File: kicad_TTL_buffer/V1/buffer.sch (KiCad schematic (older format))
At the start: 19 parts, among them P1 Conn_02x06_Odd_Even, P2 Conn_01x04, P3 Conn_01x06, P4 Conn_01x03_ODD, P5 Conn_01x03_EVEN, P6 Conn_01x01, P7 Conn_01x01, U1 74LS08

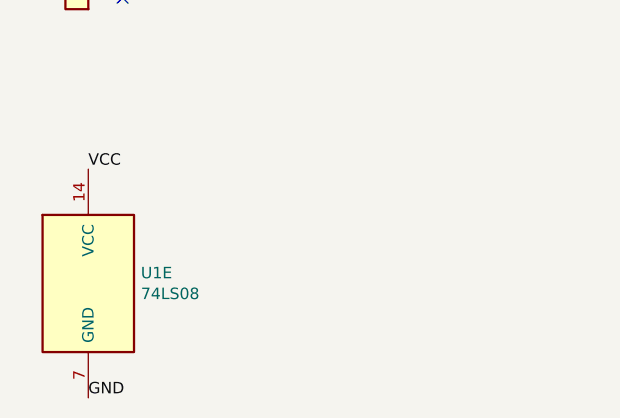
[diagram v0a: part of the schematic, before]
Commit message: Update TTL V1 board
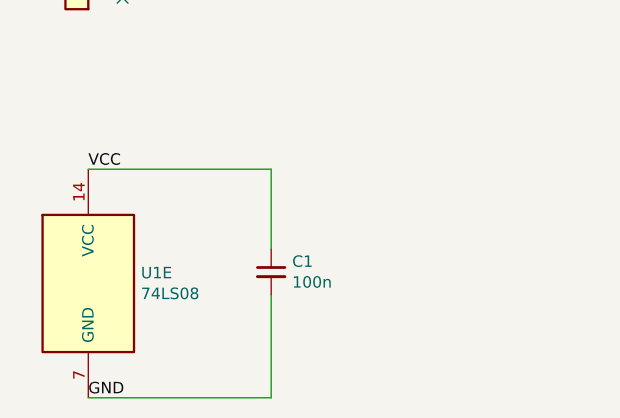
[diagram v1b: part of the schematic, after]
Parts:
- added C1: 100n, Capacitor_SMD:C_0805_2012Metric_Pad1.15x1.40mm_HandSolder, symbol Device:C_Small
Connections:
- net GND: now also C1.2
- net VCC: now also C1.1
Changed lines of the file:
@@
 Text Notes 850  4200 0    50   ~ 0
 R5 Not Fitted
+$Comp
+L Device:C_Small C1
+U 1 1 5E5AAE44
+P 1950 6250
+F 0 "C1" H 2042 6296 50  0000 L CNN
+F 1 "100n" H 2042 6205 50  0000 L CNN
+F 2 "Capacitor_SMD:C_0805_2012Metric_Pad1.15x1.40mm_HandSolder" H 1950 6250 50  0001 C CNN
+F 3 "~" H 1950 6250 50  0001 C CNN
+	1    1950 6250
+	1    0    0    -1
+$EndComp
+Wire Wire Line
+	1150 5800 1950 5800
+Wire Wire Line
+	1950 5800 1950 6150
+Wire Wire Line
+	1150 6800 1950 6800
+Wire Wire Line
+	1950 6800 1950 6350
 $EndSCHEMATC

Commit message: Extend P4 pads on TTL board
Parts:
- P3: footprint Connector_Molex:Molex_PicoBlade_53048-0610_1x06_P1.25mm_Horizontal -> Connector_Molex:Molex_PicoBlade_53048-0610_1x06_P1.25mm_Horizontal_Custom2
- P4: footprint Connector_Harwin:Harwin_M20-89003xx_1x03_P2.54mm_Horizontal_Custom_ODD -> Connector_Harwin:Harwin_M20-89003xx_1x03_P2.54mm_Horizontal_Custom_ODD2
- P5: footprint Connector_Harwin:Harwin_M20-89003xx_1x03_P2.54mm_Horizontal_Custom_EVEN -> Connector_Harwin:Harwin_M20-89003xx_1x03_P2.54mm_Horizontal_Custom_EVEN2
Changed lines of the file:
@@
 F 0 "P3" H 2168 3275 50  0000 C CNN
 F 1 "Conn_01x06" H 2168 3366 50  0000 C CNN
-F 2 "Connector_Molex:Molex_PicoBlade_53048-0610_1x06_P1.25mm_Horizontal" H 2250 3800 50  0001 C CNN
+F 2 "Connector_Molex:Molex_PicoBlade_53048-0610_1x06_P1.25mm_Horizontal_Custom2" H 2250 3800 50  0001 C CNN
 F 3 "~" H 2250 3800 50  0001 C CNN
 	1    2250 3800
@@
 F 0 "P5" H 1750 2850 50  0000 C CNN
 F 1 "Conn_01x03_EVEN" H 1450 2950 50  0000 C CNN
-F 2 "Connector_Harwin:Harwin_M20-89003xx_1x03_P2.54mm_Horizontal_Custom_EVEN" H 1750 2600 50  0001 C CNN
+F 2 "Connector_Harwin:Harwin_M20-89003xx_1x03_P2.54mm_Horizontal_Custom_EVEN2" H 1750 2600 50  0001 C CNN
 F 3 "~" H 1750 2600 50  0001 C CNN
 	1    1750 2600
@@
 F 0 "P4" H 1550 2350 50  0000 L CNN
 F 1 "Conn_01x03_ODD" H 1000 2250 50  0000 L CNN
-F 2 "Connector_Harwin:Harwin_M20-89003xx_1x03_P2.54mm_Horizontal_Custom_ODD" H 1600 2600 50  0001 C CNN
+F 2 "Connector_Harwin:Harwin_M20-89003xx_1x03_P2.54mm_Horizontal_Custom_ODD2" H 1600 2600 50  0001 C CNN
 F 3 "~" H 1600 2600 50  0001 C CNN
 	1    1600 2600
